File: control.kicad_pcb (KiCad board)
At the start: 4 copper layers, 111.9 x 109.5 mm, 175 parts, among them J1 Wurth_THR_Terminal_M4, J10 Conn_02x20_Odd_Even, J11 Conn_ARM_JTAG_SWD_10, J12 TE_Faston_20-16AWG_Straight_T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, J13 TE_Faston_20-16AWG_Straight_T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, J14 TE_Faston_20-16AWG_Straight_T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, J15 TE_Faston_20-16AWG_Straight_T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, J16 TE_Faston_20-16AWG_Straight_T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, J17 TE_Faston_20-16AWG_Straight_T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, J18 TE_Faston_20-16AWG_Straight_T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, J19 TE_Faston_20-16AWG_Straight_T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, J2 Wurth_THR_Terminal_M4, J20 TE_Faston_20-16AWG_Straight_T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, J21 TE_Faston_20-16AWG_Straight_T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, J22 TE_Faston_20-16AWG_Straight_T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, J23 TE_Faston_20-16AWG_Straight_T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, J24 TE_Faston_20-16AWG_Straight_T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, J25 TE_Faston_20-16AWG_Straight_T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, J26 TE_Faston_20-16AWG_Straight_T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, J27 TE_Faston_20-16AWG_Straight_T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, J28 Conn_01x02, J3 Conn_02x08_Odd_Even, J4 Conn_02x08_Odd_Even, J5 Conn_02x08_Odd_Even, J6 Conn_02x08_Odd_Even, J7 Conn_02x08_Odd_Even, SW1 SW_Push, U1 TPS7B8733, U2 MAX33071, U3 ATSAMD21J18A-A, U4 TCMT4600, U5 TCMT4600, U6 TCMT4600, U7 TCMT4600, U8 TCMT4600, U9 TCMT4600, Y1 32.768kHz

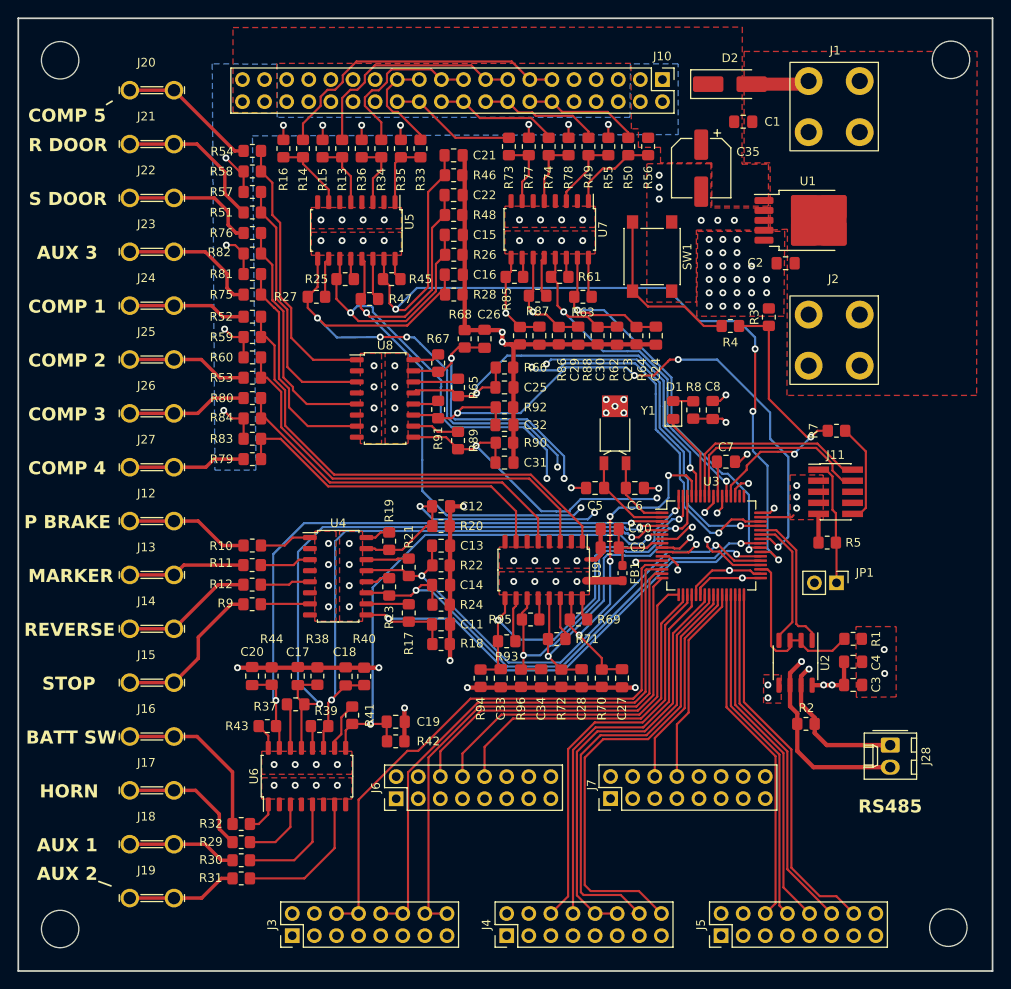
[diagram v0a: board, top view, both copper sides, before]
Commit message: update layout and add some series resistors
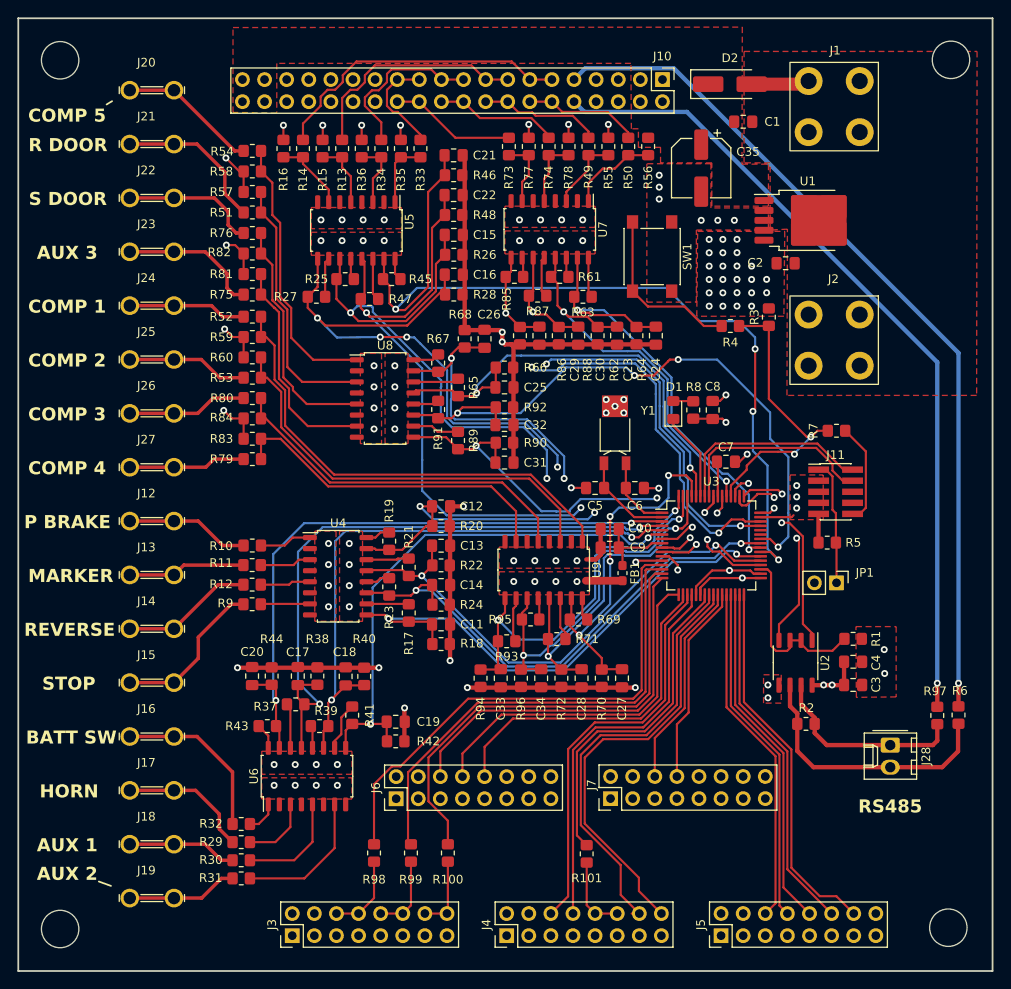
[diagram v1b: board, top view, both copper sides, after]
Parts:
- added R100: DNP, Resistor_SMD:R_0805_2012Metric_Pad1.20x1.40mm_HandSolder, F.Cu at (120.2, 138.3)
- added R101: DNP, Resistor_SMD:R_0805_2012Metric_Pad1.20x1.40mm_HandSolder, F.Cu at (136.2, 138.4)
- added R6: 0, Resistor_SMD:R_0805_2012Metric_Pad1.20x1.40mm_HandSolder, F.Cu at (178.9, 122.5)
- added R97: 0, Resistor_SMD:R_0805_2012Metric_Pad1.20x1.40mm_HandSolder, F.Cu at (176.5, 122.5)
- added R98: DNP, Resistor_SMD:R_0805_2012Metric_Pad1.20x1.40mm_HandSolder, F.Cu at (111.8, 138.3)
- added R99: DNP, Resistor_SMD:R_0805_2012Metric_Pad1.20x1.40mm_HandSolder, F.Cu at (116.0, 138.3)
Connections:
- J10 pad 10: /RS485_A -> Net-(J10-Pin_10)
- J10 pad 9: /RS485_B -> Net-(J10-Pin_9)
- J3 pad 10: FLOOD_R_EN -> Net-(J3-Pin_10)
- J3 pad 12: FLOOD_R_EN -> Net-(J3-Pin_10)
- J3 pad 14: FLOOD_P_EN -> Net-(J3-Pin_14)
- J3 pad 16: FLOOD_P_EN -> Net-(J3-Pin_14)
- J3 pad 6: FLOOD_D_EN -> Net-(J3-Pin_6)
- J3 pad 8: FLOOD_D_EN -> Net-(J3-Pin_6)
- J4 pad 10: FOG_LGT_EN -> Net-(J4-Pin_10)
- J4 pad 12: FOG_LGT_EN -> Net-(J4-Pin_10)
- U2 pad 1: UART3_RX -> UART5_RX
- U2 pad 4: UART3_TX -> UART5_TX
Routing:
- net Net-(J10-Pin_9): track 0.00 -> 98.9 mm, vias 0 -> 1
- net /RS485_B: track 118.8 -> 22.9 mm, vias 1 -> 0
- net Net-(J10-Pin_10): track 0.00 -> 93.8 mm, vias 0 -> 1
- net /RS485_A: track 119.2 -> 31.0 mm, vias 1 -> 0
- net UART5_RX: track 0.00 -> 24.6 mm, vias 0 -> 2
- net UART5_TX: track 0.00 -> 23.4 mm, vias 0 -> 2
- net UART3_RX: track 16.7 -> 0.00 mm
- net UART3_TX: track 15.3 -> 0.00 mm
- net FLOOD_D_EN: track 69.8 -> 58.6 mm
- net FOG_LGT_EN: track 49.3 -> 38.5 mm
- net FLOOD_R_EN: track 66.0 -> 55.4 mm
- net FLOOD_P_EN: track 63.9 -> 54.2 mm
- net Net-(J3-Pin_6): track 0.00 -> 9.24 mm
- net Net-(J3-Pin_14): track 0.00 -> 9.13 mm
- net Net-(J3-Pin_10): track 0.00 -> 8.89 mm
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- added copper zone on In2.Cu, net +12V
- removed copper zone on B.Cu, net +12V

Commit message: add IO expander and additional AUX outputs
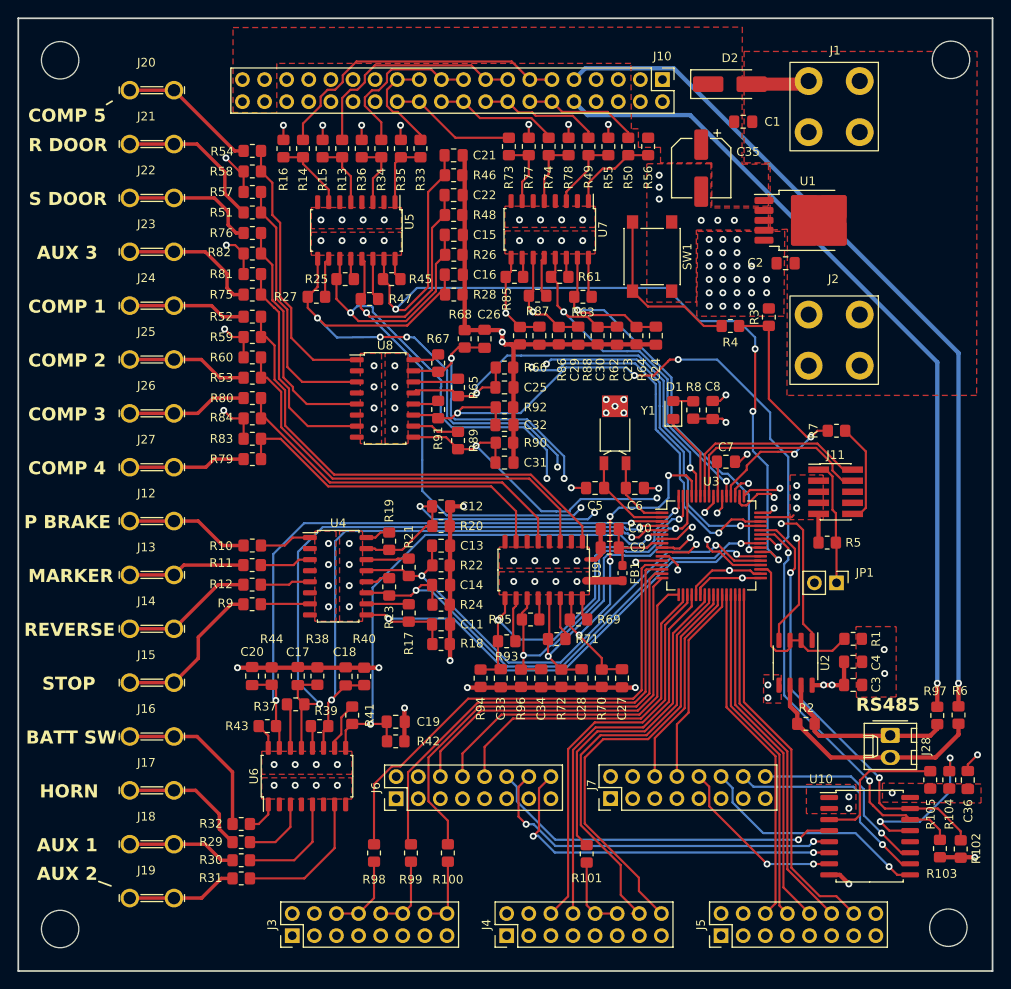
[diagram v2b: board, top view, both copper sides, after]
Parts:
- added C36: 0.1uF, Capacitor_SMD:C_0805_2012Metric_Pad1.18x1.45mm_HandSolder, F.Cu at (180.0, 129.9)
- added R102: 39, Resistor_SMD:R_0805_2012Metric_Pad1.20x1.40mm_HandSolder, F.Cu at (179.2, 137.9)
- added R103: 39, Resistor_SMD:R_0805_2012Metric_Pad1.20x1.40mm_HandSolder, F.Cu at (176.8, 137.8)
- added R104: 100K, Resistor_SMD:R_0805_2012Metric_Pad1.20x1.40mm_HandSolder, F.Cu at (177.9, 129.9)
- added R105: 100K, Resistor_SMD:R_0805_2012Metric_Pad1.20x1.40mm_HandSolder, F.Cu at (175.7, 129.9)
- added U10: PCA9358, Package_SO:SOIC-16W_7.5x10.3mm_P1.27mm, F.Cu at (168.7, 136.4)
- moved J28 1.12 mm to (171.1, 124.8)
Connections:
- J6 pad 12: unconnected-(J6-Pin_12-Pad12) -> AUX_4_EN
- J6 pad 14: unconnected-(J6-Pin_14-Pad14) -> AUX_5_EN
- J6 pad 16: unconnected-(J6-Pin_16-Pad16) -> AUX_6_EN
- J7 pad 10: unconnected-(J7-Pin_10-Pad10) -> AUX_9_EN
- J7 pad 12: unconnected-(J7-Pin_12-Pad12) -> AUX_10_EN
- J7 pad 14: unconnected-(J7-Pin_14-Pad14) -> AUX_11_EN
- J7 pad 16: unconnected-(J7-Pin_16-Pad16) -> AUX_12_EN
- J7 pad 6: AUX_4_EN -> AUX_7_EN
- J7 pad 8: AUX_5_EN -> AUX_8_EN
- U3 pad 26: AUX_4_EN -> AUX_7_EN
- U3 pad 27: AUX_5_EN -> AUX_8_EN
- U3 pad 43: UART3_TX -> I2C3_SCL
- U3 pad 44: UART3_RX -> I2C3_SDA
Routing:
- net I2C3_SDA: track 0.00 -> 50.2 mm, vias 0 -> 2
- net I2C3_SCL: track 0.00 -> 48.1 mm, vias 0 -> 2
- net AUX_6_EN: track 0.00 -> 42.7 mm, vias 0 -> 2
- net AUX_10_EN: track 0.00 -> 27.4 mm, vias 0 -> 1
- net AUX_11_EN: track 0.00 -> 25.3 mm, vias 0 -> 1
- net AUX_7_EN: track 0.00 -> 23.9 mm
- net AUX_8_EN: track 0.00 -> 23.0 mm
- net AUX_12_EN: track 0.00 -> 22.0 mm, vias 0 -> 1
- net AUX_9_EN: track 0.00 -> 20.4 mm, vias 0 -> 2
- net AUX_5_EN: track 23.0 -> 42.6 mm, vias 0 -> 2
- net Net-(U10-INT#): track 0.00 -> 18.7 mm, vias 0 -> 2
- net AUX_4_EN: track 23.9 -> 41.5 mm, vias 0 -> 1
- net Net-(U10-RESET#): track 0.00 -> 16.2 mm
- net GNDREF: track 149.4 -> 154.4 mm, vias 58 -> 62
- net +3.3V: track 120.4 -> 124.4 mm, vias 54 -> 56
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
